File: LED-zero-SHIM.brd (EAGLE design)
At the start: 30 x 65 mm, 148 parts

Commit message: added buffer and caps
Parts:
- added C1, C2, C3, C4: 10uF, rcl:C0805
- added IC1: TXB0101DCKR, TXB0101DCKR:SOT65P210X110-6N
- added R1: (no value), rcl:R0402
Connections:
- new net DATA: IC1.3
- new net N$143: IC1.5, R1.2
- net 3.3V: now also IC1.1, R1.1
- net 5V: now also C1.1, C2.1, C3.1, C4.1, IC1.6
- net DI_FIRST: now also IC1.4
- net GND: now also C1.2, C2.2, C3.2, C4.2, IC1.2
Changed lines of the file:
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@@
 <attribute name="VALUE" x="0.635" y="9.906" size="0.6096" layer="51" font="vector" rot="R270"/>
+</element>
+<element name="IC1" library="TXB0101DCKR" package="SOT65P210X110-6N" value="TXB0101DCKR" x="21.082" y="60.071" smashed="yes">
+<attribute name="NAME" x="18.582" y="61.571" size="0.6096" layer="25" font="vector"/>
+<attribute name="VALUE" x="18.582" y="58.571" size="0.6096" layer="27" font="vector" align="top-left"/>
+</element>
+<element name="R1" library="rcl" library_urn="urn:adsk.eagle:library:334" package="R0402" package3d_urn="urn:adsk.eagle:package:23547/3" value="" x="21.082" y="62.103" smashed="yes">
+<attribute name="NAME" x="20.447" y="62.738" size="0.6096" layer="25" font="vector"/>
+<attribute name="POPULARITY" value="0" x="21.082" y="62.103" size="1.778" layer="27" display="off"/>
+<attribute name="SPICEPREFIX" value="R" x="21.082" y="62.103" size="1.778" layer="27" display="off"/>
+<attribute name="VALUE" x="20.447" y="60.198" size="1.27" layer="27"/>
+</element>
+<element name="C1" library="rcl" library_urn="urn:adsk.eagle:library:334" package="C0805" package3d_urn="urn:adsk.eagle:package:23617/2" value="10uF" x="16.51" y="60.706" smashed="yes" rot="R90">
+<attribute name="NAME" x="15.24" y="59.436" size="0.6096" layer="25" font="vector" rot="R90"/>
+<attribute name="POPULARITY" value="88" x="16.51" y="60.706" size="1.778" layer="27" rot="R90" display="off"/>
+<attribute name="SPICEPREFIX" value="C" x="16.51" y="60.706" size="1.778" layer="27" rot="R90" display="off"/>
+<attribute name="VALUE" x="19.05" y="59.436" size="0.6096" layer="27" font="vector" rot="R90"/>
+</element>
+<element name="C2" library="rcl" library_urn="urn:adsk.eagle:library:334" package="C0805" package3d_urn="urn:adsk.eagle:package:23617/2" value="10uF" x="10.922" y="60.706" smashed="yes" rot="R90">
+<attribute name="NAME" x="9.652" y="59.436" size="0.6096" layer="25" font="vector" rot="R90"/>
+<attribute name="POPULARITY" value="88" x="10.922" y="60.706" size="1.778" layer="27" rot="R90" display="off"/>
+<attribute name="SPICEPREFIX" value="C" x="10.922" y="60.706" size="1.778" layer="27" rot="R90" display="off"/>
+<attribute name="VALUE" x="13.462" y="59.436" size="0.6096" layer="27" font="vector" rot="R90"/>
+</element>
+<element name="C3" library="rcl" library_urn="urn:adsk.eagle:library:334" package="C0805" package3d_urn="urn:adsk.eagle:package:23617/2" value="10uF" x="19.304" y="4.064" smashed="yes" rot="R270">
+<attribute name="NAME" x="20.574" y="5.334" size="0.6096" layer="25" font="vector" rot="R270"/>
+<attribute name="POPULARITY" value="88" x="19.304" y="4.064" size="1.778" layer="27" rot="R270" display="off"/>
+<attribute name="SPICEPREFIX" value="C" x="19.304" y="4.064" size="1.778" layer="27" rot="R270" display="off"/>
+<attribute name="VALUE" x="16.764" y="5.334" size="0.6096" layer="27" font="vector" rot="R270"/>
+</element>
+<element name="C4" library="rcl" library_urn="urn:adsk.eagle:library:334" package="C0805" package3d_urn="urn:adsk.eagle:package:23617/2" value="10uF" x="10.922" y="4.064" smashed="yes" rot="R270">
+<attribute name="NAME" x="12.192" y="5.334" size="0.6096" layer="25" font="vector" rot="R270"/>
+<attribute name="POPULARITY" value="88" x="10.922" y="4.064" size="1.778" layer="27" rot="R270" display="off"/>
+<attribute name="SPICEPREFIX" value="C" x="10.922" y="4.064" size="1.778" layer="27" rot="R270" display="off"/>
+<attribute name="VALUE" x="8.382" y="5.334" size="0.6096" layer="27" font="vector" rot="R270"/>
 </element>
 </elements>
@@
 <contactref element="LED143" pad="GND"/>
 <contactref element="LED144" pad="GND"/>
+<contactref element="IC1" pad="2"/>
+<contactref element="C1" pad="2"/>
+<contactref element="C2" pad="2"/>
+<contactref element="C3" pad="2"/>
+<contactref element="C4" pad="2"/>
 </signal>
 <signal name="3.3V">
 <contactref element="J3" pad="1"/>
 <contactref element="J3" pad="9"/>
+<contactref element="IC1" pad="1"/>
+<contactref element="R1" pad="1"/>
+<wire x1="20.122" y1="60.721" x2="25.4318" y2="56.615" width="0" layer="19" extent="1-1"/>
+<wire x1="20.582" y1="62.103" x2="20.122" y2="60.721" width="0" layer="19" extent="1-1"/>
 <wire x1="25.4318" y1="36.295" x2="25.4318" y2="56.615" width="0" layer="19" extent="1-1"/>
 </signal>
@@
 <contactref element="LED143" pad="VDD"/>
 <contactref element="LED144" pad="VDD"/>
+<contactref element="IC1" pad="6"/>
+<contactref element="C1" pad="1"/>
+<contactref element="C2" pad="1"/>
+<contactref element="C3" pad="1"/>
+<contactref element="C4" pad="1"/>
 <wire x1="27.6162" y1="54.075" x2="27.9718" y2="56.615" width="0" layer="19" extent="1-1"/>
 <wire x1="21.548" y1="54.255" x2="27.6162" y2="54.075" width="0" layer="19" extent="1-1"/>
@@
 <wire x1="18.754" y1="54.255" x2="21.548" y2="54.255" width="0" layer="19" extent="1-1"/>
 <wire x1="15.96" y1="57.049" x2="18.754" y2="57.049" width="0" layer="19" extent="1-1"/>
+<wire x1="16.51" y1="59.756" x2="15.96" y2="57.049" width="0" layer="19" extent="1-1"/>
 <wire x1="21.548" y1="48.667" x2="21.548" y2="51.461" width="0" layer="19" extent="1-1"/>
 <wire x1="18.754" y1="51.461" x2="21.548" y2="51.461" width="0" layer="19" extent="1-1"/>
@@
 <wire x1="13.166" y1="54.255" x2="15.96" y2="54.255" width="0" layer="19" extent="1-1"/>
 <wire x1="10.372" y1="57.049" x2="13.166" y2="57.049" width="0" layer="19" extent="1-1"/>
+<wire x1="10.922" y1="59.756" x2="10.372" y2="57.049" width="0" layer="19" extent="1-1"/>
 <wire x1="18.754" y1="45.873" x2="21.548" y2="45.873" width="0" layer="19" extent="1-1"/>
 <wire x1="15.96" y1="48.667" x2="18.754" y2="48.667" width="0" layer="19" extent="1-1"/>
@@
 <wire x1="1.99" y1="12.345" x2="4.784" y2="12.345" width="0" layer="19" extent="1-1"/>
 <wire x1="1.99" y1="9.551" x2="4.784" y2="9.551" width="0" layer="19" extent="1-1"/>
+<wire x1="22.042" y1="60.721" x2="21.548" y2="57.049" width="0" layer="19" extent="1-1"/>
+<wire x1="19.304" y1="5.014" x2="18.754" y2="9.551" width="0" layer="19" extent="1-1"/>
+<wire x1="10.922" y1="5.014" x2="10.372" y2="9.551" width="0" layer="19" extent="1-1"/>
 </signal>
 <signal name="GND1" airwireshidden="yes">
@@
 <signal name="DI_FIRST">
 <contactref element="LED1" pad="DI"/>
+<contactref element="IC1" pad="4"/>
+<wire x1="22.648" y1="57.049" x2="22.042" y2="59.421" width="0" layer="19" extent="1-1"/>
 </signal>
 <signal name="N$11">
@@
 <signal name="DO_LAST">
 <contactref element="LED144" pad="DO"/>
+</signal>
+<signal name="DATA">
+<contactref element="IC1" pad="3"/>
+</signal>
+<signal name="N$143">
+<contactref element="R1" pad="2"/>
+<contactref element="IC1" pad="5"/>
+<wire x1="22.042" y1="60.071" x2="21.582" y2="62.103" width="0" layer="19" extent="1-1"/>
 </signal>
 </signals>
@@
 </board>
 </drawing>
+<compatibility>
+<note version="8.2" severity="warning">
+Since Version 8.2, EAGLE supports online libraries. The ids
+of those online libraries will not be understood (or retained)
+with this version.
+</note>
+<note version="8.3" severity="warning">
+Since Version 8.3, EAGLE supports URNs for individual library
+assets (packages, symbols, and devices). The URNs of those assets
+will not be understood (or retained) with this version.
+</note>
+<note version="8.3" severity="warning">
+Since Version 8.3, EAGLE supports the association of 3D packages
+with devices in libraries, schematics, and board files. Those 3D
+packages will not be understood (or retained) with this version.
+</note>
+</compatibility>
 </eagle>

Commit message: Added solder joint for DATA input configuration
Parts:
- added SJ1: (no value), _my_jumpers:SJ_3
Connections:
- net DATA: now also SJ1.2
- net GPIO10: now also SJ1.3
- net GPIO18: now also SJ1.1
- net GPIO21: now also SJ1.4
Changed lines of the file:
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@@
 <attribute name="VALUE" x="8.382" y="5.334" size="0.6096" layer="27" font="vector" rot="R270"/>
+</element>
+<element name="SJ1" library="_my_jumpers" package="SJ_3" value="" x="20.066" y="60.706" smashed="yes" rot="MR270">
+<attribute name="NAME" x="18.796" y="63.119" size="0.6096" layer="26" font="vector" ratio="10" rot="MR270"/>
 </element>
 </elements>
@@
 <signal name="GPIO10">
 <contactref element="J3" pad="10"/>
+<contactref element="SJ1" pad="3"/>
+<wire x1="20.066" y1="59.055" x2="25.0762" y2="33.755" width="0" layer="19" extent="1-1"/>
 </signal>
 <signal name="GPIO9">
@@
 <signal name="GPIO18">
 <contactref element="J4" pad="6"/>
+<contactref element="SJ1" pad="1"/>
+<wire x1="20.066" y1="62.357" x2="27.6162" y2="43.915" width="0" layer="19" extent="1-1"/>
 </signal>
 <signal name="GPIO23">
@@
 <signal name="GPIO21">
 <contactref element="J4" pad="20"/>
+<contactref element="SJ1" pad="4"/>
+<wire x1="21.717" y1="60.706" x2="27.6162" y2="8.355" width="0" layer="19" extent="1-1"/>
 </signal>
 <signal name="5V">
@@
 <signal name="DATA">
 <contactref element="IC1" pad="3"/>
+<contactref element="SJ1" pad="2"/>
+<wire x1="20.066" y1="60.706" x2="20.122" y2="59.421" width="0" layer="19" extent="1-1"/>
 </signal>
 <signal name="N$143">

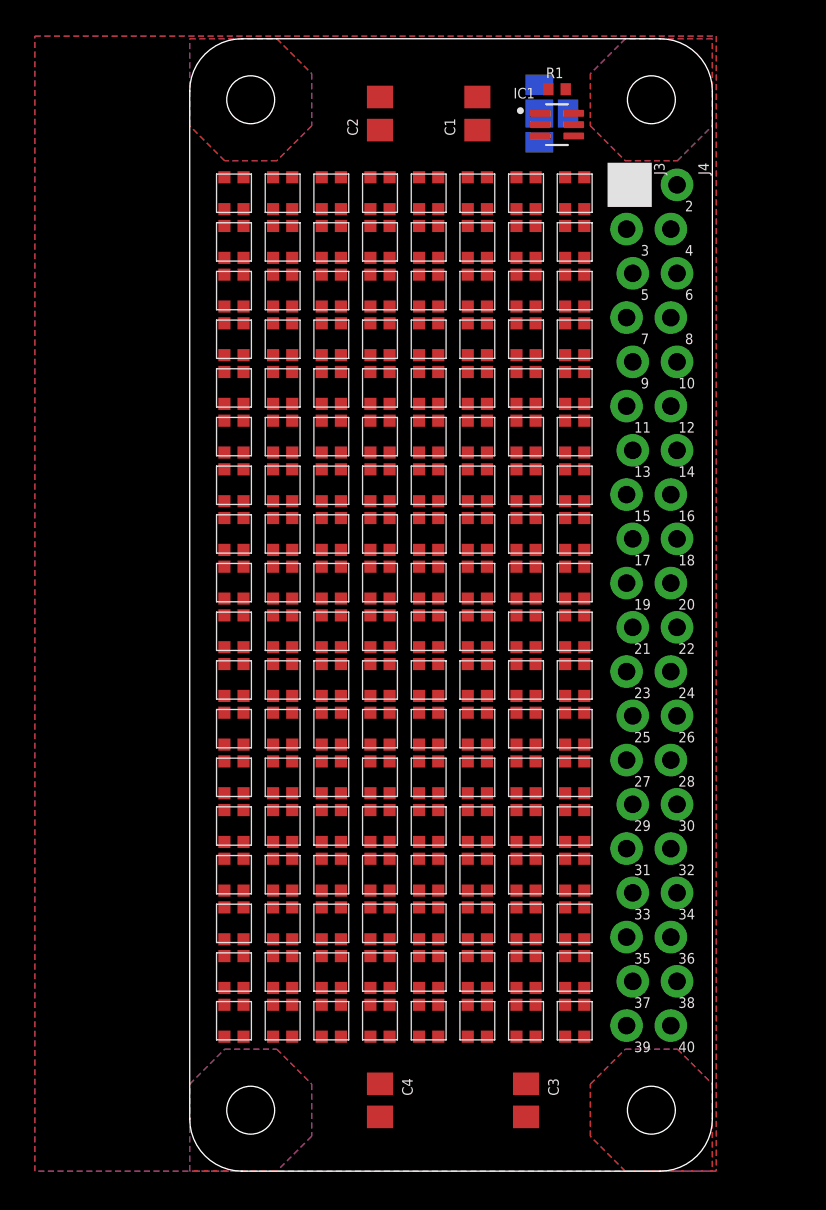
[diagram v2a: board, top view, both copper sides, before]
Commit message: Use C veriant of LED insted of B.
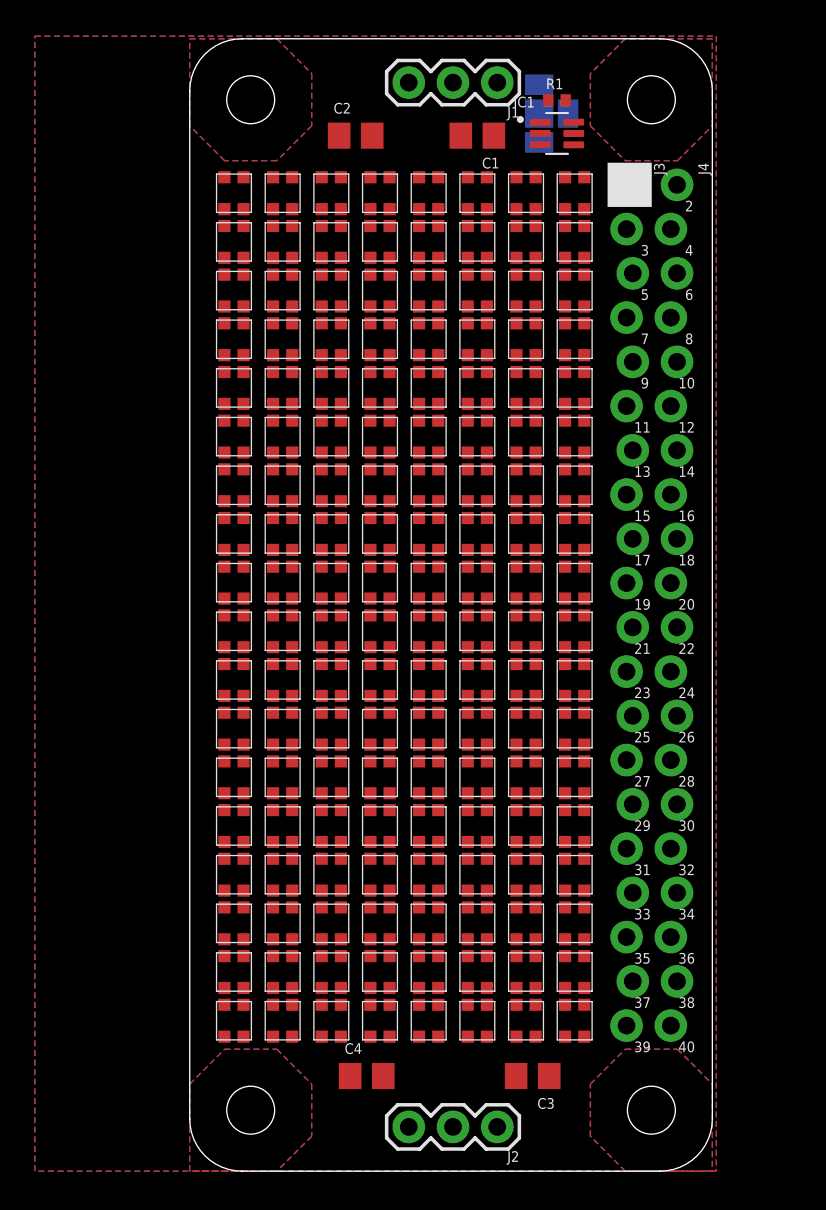
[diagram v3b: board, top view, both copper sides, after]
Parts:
- added J1, J2: (no value), SparkFun-Connectors:1X03
- LED1, LED10, LED100, LED101, LED102, LED103, LED104, LED105, LED106, LED107, LED108, LED109, LED11, LED110, LED111, LED112, LED113, LED114, LED115, LED116, LED117, LED118, LED119, LED12, LED120, LED121, LED122, LED123, LED124, LED125, LED126, LED127, LED128, LED129, LED13, LED130, LED131, LED132, LED133, LED134, LED135, LED136, LED137, LED138, LED139, LED14, LED140, LED141, LED142, LED143, LED144, LED15, LED16, LED17, LED18, LED19, LED2, LED20, LED21, LED22, LED23, LED24, LED25, LED26, LED27, LED28, LED29, LED3, LED30, LED31, LED32, LED33, LED34, LED35, LED36, LED37, LED38, LED39, LED4, LED40, LED41, LED42, LED43, LED44, LED45, LED46, LED47, LED48, LED49, LED5, LED50, LED51, LED52, LED53, LED54, LED55, LED56, LED57, LED58, LED59, LED6, LED60, LED61, LED62, LED63, LED64, LED65, LED66, LED67, LED68, LED69, LED7, LED70, LED71, LED72, LED73, LED74, LED75, LED76, LED77, LED78, LED79, LED8, LED80, LED81, LED82, LED83, LED84, LED85, LED86, LED87, LED88, LED89, LED9, LED90, LED91, LED92, LED93, LED94, LED95, LED96, LED97, LED98, LED99: value WS2812B-2020 -> WS2812C-2020; device WS2812B-2020:WS2812B-2020 -> WS281X:WS2812X-2020
- moved C2 1.89 mm to (9.53, 59.4), turned to 0 degrees
- moved C4 1.59 mm to (10.2, 5.46), turned to 0 degrees
- moved C3 1.45 mm to (19.7, 5.46), turned to 180 degrees
- moved C1 1.27 mm to (16.5, 59.4), turned to 180 degrees
- moved R1 0.63 mm to (21.1, 61.5)
- moved IC1 0.51 mm to (21.1, 59.6)
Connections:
- net 5V: now also J1.3, J2.3
- net DI_FIRST: now also J1.2
- net DO_LAST: now also J2.2
- net GND: now also J1.1, J2.1

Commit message: Added some traces.
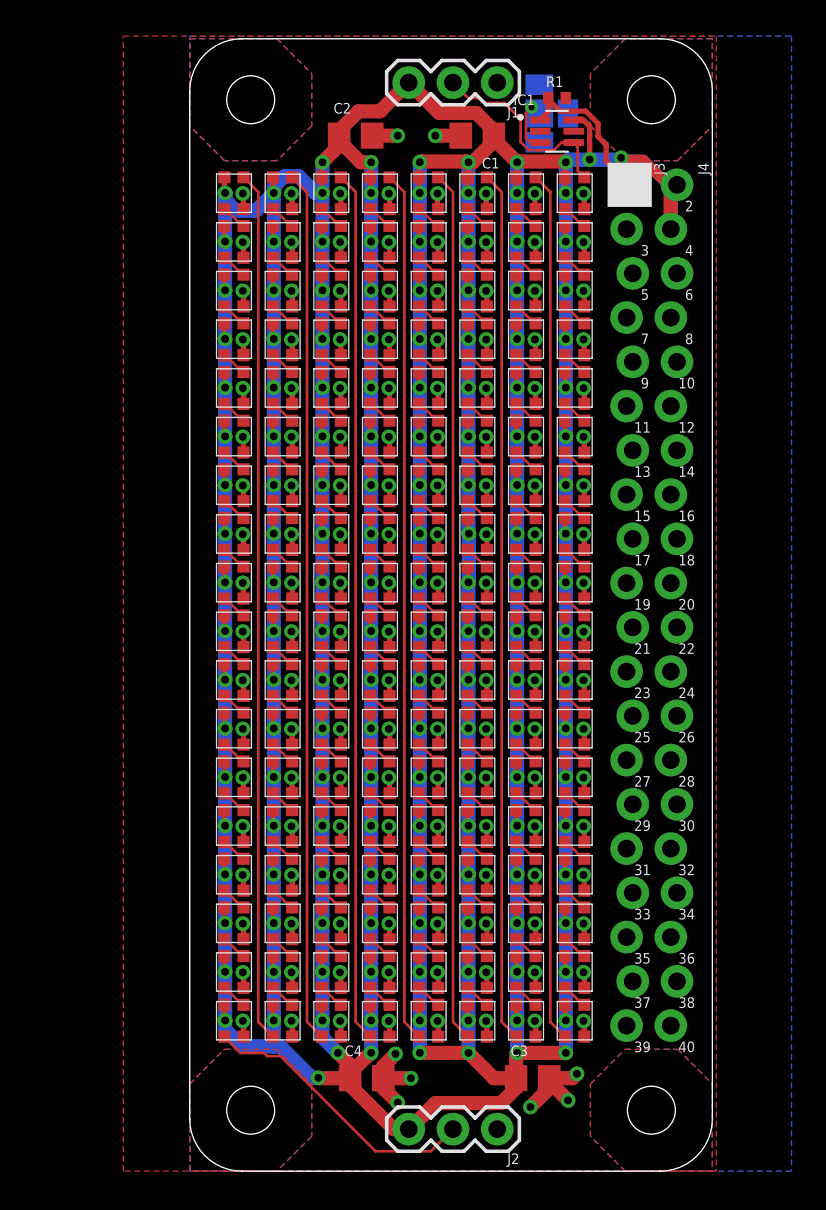
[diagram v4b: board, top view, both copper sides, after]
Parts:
- R1: value (none) -> 10K
- moved C3 0.13 mm to (19.7, 5.33), turned to 0 degrees
- moved C4 0.13 mm to (10.2, 5.33)
- moved J2 0.13 mm to (17.7, 2.41)
- moved IC1 0.13 mm to (21.1, 59.7)
- moved R1 0.13 mm to (21.1, 61.6)
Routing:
- net 5V: track 0.00 -> 629.1 mm, vias 0 -> 159
- net GND: track 0.00 -> 145.7 mm, vias 0 -> 152
- net N$89: track 0.00 -> 50.0 mm
- net N$54: track 0.00 -> 50.0 mm
- net N$36: track 0.00 -> 50.0 mm
- net N$18: track 0.00 -> 50.0 mm
- net N$125: track 0.00 -> 50.0 mm
- net N$107: track 0.00 -> 50.0 mm
- net DO_MID: track 0.00 -> 50.0 mm
- net DO_LAST: track 0.00 -> 16.4 mm
- net DI_FIRST: track 0.00 -> 11.7 mm
- net 3.3V: track 0.00 -> 9.39 mm
- net DATA: track 0.00 -> 3.43 mm, vias 0 -> 1
- net N$4: track 0.00 -> 1.50 mm
- net N$6: track 0.00 -> 1.50 mm
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
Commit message: Made the board 4-layer and routed it completely.
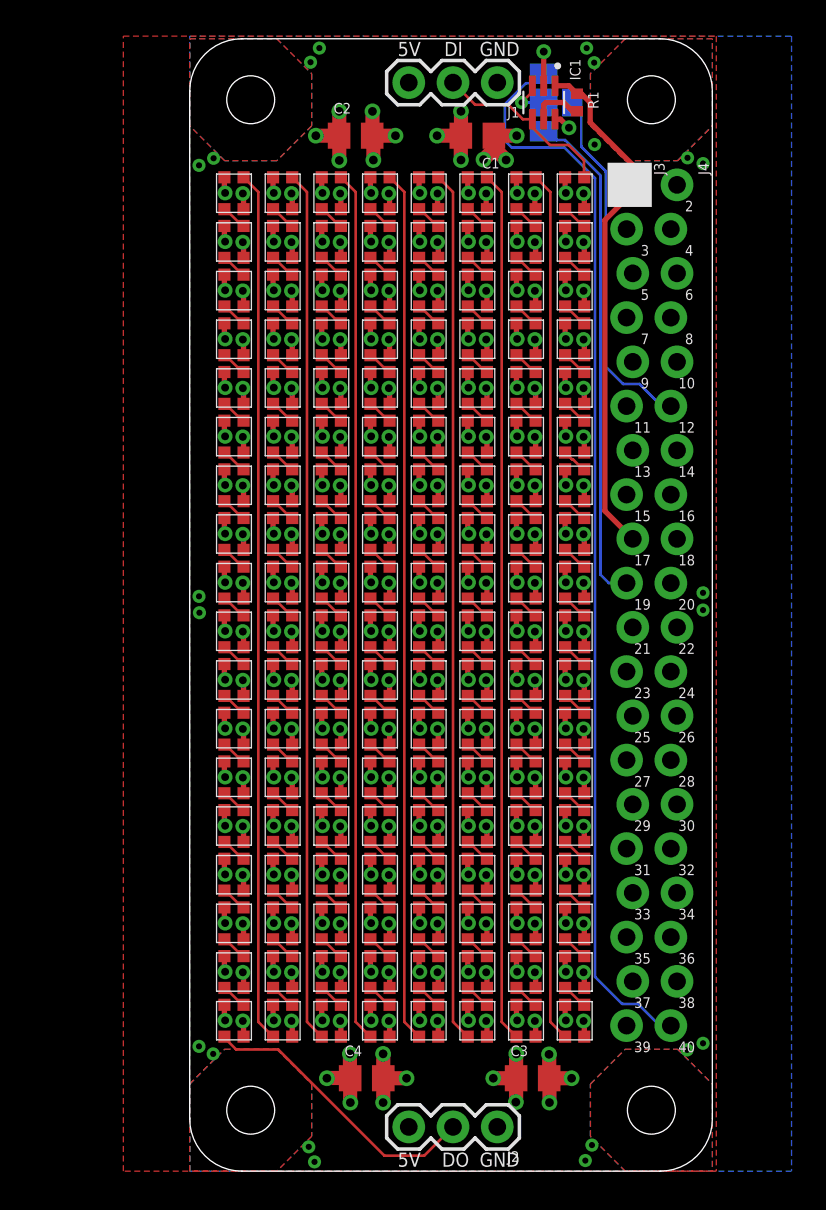
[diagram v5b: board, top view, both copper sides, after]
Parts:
- moved IC1 1.82 mm to (20.3, 61.3), turned to 270 degrees
- moved R1 1.17 mm to (22.2, 61.3), turned to 270 degrees
- moved SJ1 0.68 mm to (20.3, 61.3)
- moved J2 0.13 mm to (17.7, 2.54)
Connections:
- net GPIO18: now also SJ1.4; no longer SJ1.1
- net GPIO21: now also SJ1.1; no longer SJ1.4
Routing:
- net 5V: track 629.1 -> 150.4 mm, vias 159 -> 167
- net GPIO21: track 0.00 -> 62.5 mm
- net GPIO10: track 0.00 -> 28.9 mm
- net GPIO18: track 0.00 -> 21.8 mm
- net 3.3V: track 9.39 -> 29.8 mm
- net GND: track 145.7 -> 150.6 mm, vias 152 -> 168
- net N$143: track 0.00 -> 3.00 mm
- net DI_FIRST: track 11.7 -> 10.6 mm
- net DATA: track 3.43 -> 2.49 mm
- added copper zone on layer 1, net 5V
- added copper zone on layer 15, net 5V
- added copper zone on layer 2, net GND
- added copper zone on layer 16, net GND2
- removed copper zone on layer 1, net GND
- removed copper zone on layer 16, net GND1
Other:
- board text added: "5V"
- board text added: "DI"
- board text added: "DO"
- board text added: "GND"
- board text added: "GPIO10"
- board text added: "GPIO18"
- board text added: "GPIO21"
